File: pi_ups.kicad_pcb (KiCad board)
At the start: 2 copper layers, 92.7 x 53.3 mm, 25 parts, among them J1 Screw_Terminal_01x02, J2 Screw_Terminal_01x02, J3 Conn_02x03_Odd_Even, U1 MCP3428, U2 AP63205WU

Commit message: r0.1 board is complete
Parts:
- removed C3: 0.1u, Capacitor_SMD:C_0603_1608Metric
- removed R8: 100k, Resistor_SMD:R_0603_1608Metric
- added JP1: Jumper_2_Bridged, pi_ups:jumper_bridged_0603, B.Cu at (103.8, 97.5)
- ADR0: renamed from R7; value 0 -> Jumper_2_Bridged; footprint Resistor_SMD:R_0603_1608Metric -> pi_ups:jumper_bridged_0603; moved to B.Cu
- ADR1: renamed from R6; value 0 -> Jumper_2_Bridged; footprint Resistor_SMD:R_0603_1608Metric -> pi_ups:jumper_bridged_0603; moved to B.Cu
- J3: moved to B.Cu
- L1: footprint Inductor_SMD:L_10.4x10.4_H4.8 -> pi_ups:NRS5030
- R1, R2, R3: value 10m -> 50m
- R4: value 400k -> 1M
- moved R5 53.1 mm to (83.1, 99.8)
- moved ADR0 51.6 mm to (85.1, 91.0), turned to 90 degrees
- moved ADR1 50.9 mm to (85.1, 94.8), turned to -90 degrees
- moved U2 49.0 mm to (99.1, 94.3), turned to 90 degrees
- moved R4 48.6 mm to (83.4, 102.0), turned to 180 degrees
- moved L1 44.3 mm to (101.1, 89.4)
- moved FB1 41.6 mm to (92.7, 88.4), turned to -90 degrees
- moved C2 39.3 mm to (92.7, 91.9), turned to -90 degrees
- moved J3 39.1 mm to (109.5, 87.9), turned to 180 degrees
- moved C6 35.8 mm to (97.5, 89.9), turned to -90 degrees
- moved C1 33.3 mm to (90.2, 87.6), turned to 180 degrees
- moved C7 23.5 mm to (105.7, 92.0), turned to 90 degrees
- moved C5 22.9 mm to (102.7, 93.0)
- moved C4 19.5 mm to (103.1, 95.5)
- moved U1 9.18 mm to (87.7, 94.0)
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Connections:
- ADR0 pad 1: Net-(U1-Adr1) -> Net-(ADR0-A)
- ADR1 pad 1: Net-(U1-Adr0) -> Net-(ADR1-A)
- U1 pad 10: Net-(U1-Adr1) -> Net-(ADR1-A)
- U1 pad 9: Net-(U1-Adr0) -> Net-(ADR0-A)
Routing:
- net /GNDB: track 31.1 -> 78.6 mm
- net /SCL: track 0.00 -> 40.9 mm
- net /SDA: track 0.00 -> 35.0 mm
- net +5V: track 0.00 -> 28.3 mm
- net VCC: track 9.93 -> 35.8 mm, vias 0 -> 2
- net /Bat2_i: track 6.13 -> 31.4 mm, vias 0 -> 2
- net GND: track 0.00 -> 23.9 mm, vias 0 -> 37
- net +3.3V: track 0.00 -> 21.3 mm, vias 0 -> 1
- net Net-(JP1-A): track 0.00 -> 7.59 mm, vias 0 -> 1
- net /Bat_v: track 0.00 -> 6.76 mm
- net /Bat1_i: track 7.29 -> 13.9 mm
- net Net-(U2-SW): track 0.00 -> 5.68 mm
- net Net-(U1-VDD): track 0.00 -> 4.61 mm
- net Net-(ADR1-A): track 0.00 -> 2.79 mm, vias 0 -> 1
- net Net-(U2-BST): track 0.00 -> 2.68 mm
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- added copper zone on B.Cu, net GND
- added copper zone on F.Cu, net GND
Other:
- board size 92.7 x 53.3 mm -> 34.3 x 30 mm
- board text added: "https://github.com/kamocat/pi_ups"
- board text added: "rPi UPS v0.1 March 2023"

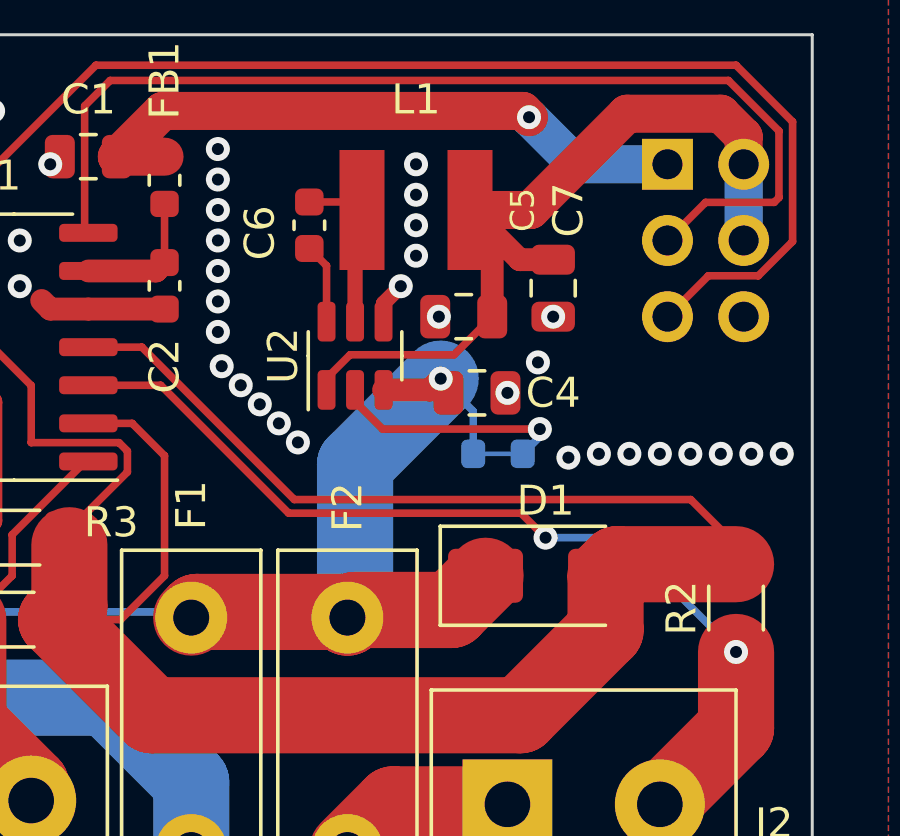
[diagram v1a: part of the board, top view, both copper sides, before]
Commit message: Minor silkscreen and package changes
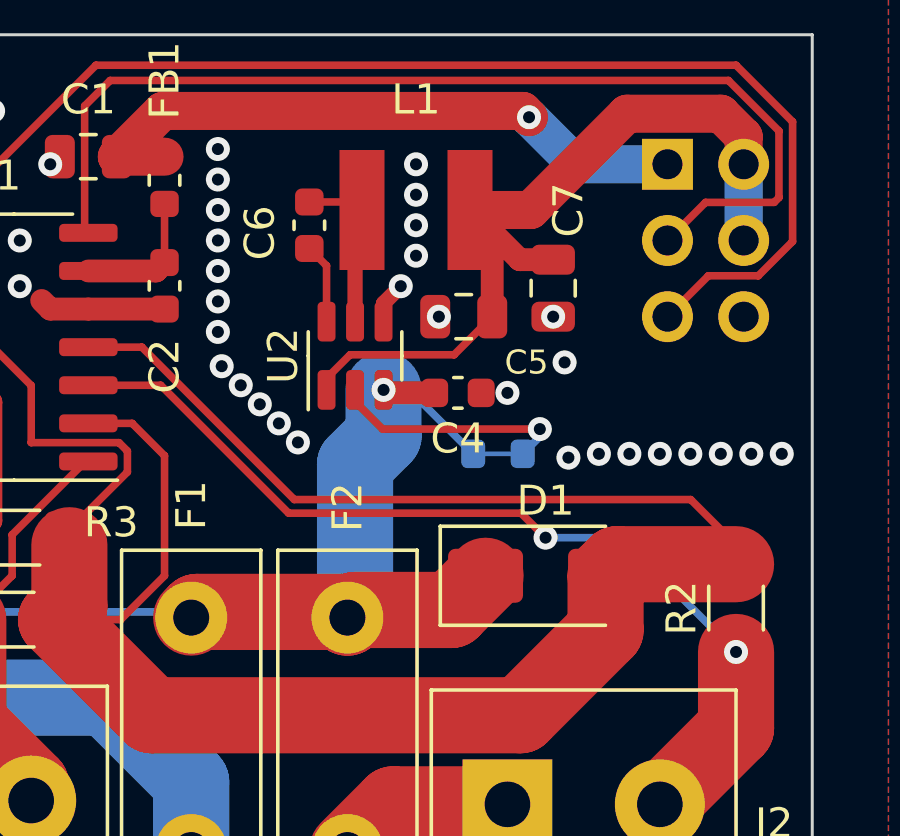
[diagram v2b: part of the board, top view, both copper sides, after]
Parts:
- C4: footprint Capacitor_SMD:C_0805_2012Metric -> Capacitor_SMD:C_0603_1608Metric
- moved C4 0.63 mm to (102.5, 95.5)
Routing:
- net VCC: track 35.8 -> 34.5 mm
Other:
- board text added: "Enable"
- board text added: "github.com/kamocat/pi_ups"
- board text removed: "https://github.com/kamocat/pi_ups"
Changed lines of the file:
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@@
     )
   )
-  (footprint "Capacitor_SMD:C_0805_2012Metric" (layer "F.Cu")
-    (at 103.124 95.504)
-    (descr "Capacitor SMD 0805 (2012 Metric), square (rectangular) end terminal, IPC_7351 nominal, (Body size source: IPC-SM-782 page 76, https://www.pcb-3d.com/wordpress/wp-content/uploads/ipc-sm-782a_amendment_1_and_2.pdf, https://docs.google.com/spreadsheets/d/1BsfQQcO9C6DZCsRaXUlFlo91Tg2WpOkGARC1WS5S8t0/edit?usp=sharing), generated with kicad-footprint-generator")
+  (footprint "Capacitor_SMD:C_0603_1608Metric" (layer "F.Cu")
+    (at 102.489 95.504)
+    (descr "Capacitor SMD 0603 (1608 Metric), square (rectangular) end terminal, IPC_7351 nominal, (Body size source: IPC-SM-782 page 76, https://www.pcb-3d.com/wordpress/wp-content/uploads/ipc-sm-782a_amendment_1_and_2.pdf), generated with kicad-footprint-generator")
     (tags "capacitor")
     (property "Sheetfile" "pi_ups.kicad_sch")
@@
     (property "ki_keywords" "cap capacitor")
     (attr smd)
-    (fp_text reference "C4" (at 2.54 0) (layer "F.SilkS")
-        (effects (font (size 1 1) (thickness 0.15)))
-    )
-    (fp_text value "10u" (at 0 1.68) (layer "F.Fab")
+    (fp_text reference "C4" (at 0 1.524) (layer "F.SilkS")
+        (effects (font (size 1 1) (thickness 0.15)))
+    )
+    (fp_text value "10u" (at 0 1.43) (layer "F.Fab")
         (effects (font (size 1 1) (thickness 0.15)))
     )
     (fp_text user "${REFERENCE}" (at 0 0) (layer "F.Fab")
-        (effects (font (size 0.5 0.5) (thickness 0.08)))
-    )
-    (fp_line (start -0.261252 -0.735) (end 0.261252 -0.735)
-      (stroke (width 0.12) (type solid)) (layer "F.SilkS"))
-    (fp_line (start -0.261252 0.735) (end 0.261252 0.735)
-      (stroke (width 0.12) (type solid)) (layer "F.SilkS"))
-    (fp_line (start -1.7 -0.98) (end 1.7 -0.98)
-      (stroke (width 0.05) (type solid)) (layer "F.CrtYd"))
-    (fp_line (start -1.7 0.98) (end -1.7 -0.98)
-      (stroke (width 0.05) (type solid)) (layer "F.CrtYd"))
-    (fp_line (start 1.7 -0.98) (end 1.7 0.98)
-      (stroke (width 0.05) (type solid)) (layer "F.CrtYd"))
-    (fp_line (start 1.7 0.98) (end -1.7 0.98)
-      (stroke (width 0.05) (type solid)) (layer "F.CrtYd"))
-    (fp_line (start -1 -0.625) (end 1 -0.625)
-      (stroke (width 0.1) (type solid)) (layer "F.Fab"))
-    (fp_line (start -1 0.625) (end -1 -0.625)
-      (stroke (width 0.1) (type solid)) (layer "F.Fab"))
-    (fp_line (start 1 -0.625) (end 1 0.625)
-      (stroke (width 0.1) (type solid)) (layer "F.Fab"))
-    (fp_line (start 1 0.625) (end -1 0.625)
-      (stroke (width 0.1) (type solid)) (layer "F.Fab"))
-    (pad "1" smd roundrect (at -0.95 0) (size 1 1.45) (layers "F.Cu" "F.Paste" "F.Mask") (roundrect_rratio 0.25)
+        (effects (font (size 0.4 0.4) (thickness 0.06)))
+    )
+    (fp_line (start -0.14058 -0.51) (end 0.14058 -0.51)
+      (stroke (width 0.12) (type solid)) (layer "F.SilkS"))
+    (fp_line (start -0.14058 0.51) (end 0.14058 0.51)
+      (stroke (width 0.12) (type solid)) (layer "F.SilkS"))
+    (fp_line (start -1.48 -0.73) (end 1.48 -0.73)
+      (stroke (width 0.05) (type solid)) (layer "F.CrtYd"))
+    (fp_line (start -1.48 0.73) (end -1.48 -0.73)
+      (stroke (width 0.05) (type solid)) (layer "F.CrtYd"))
+    (fp_line (start 1.48 -0.73) (end 1.48 0.73)
+      (stroke (width 0.05) (type solid)) (layer "F.CrtYd"))
+    (fp_line (start 1.48 0.73) (end -1.48 0.73)
+      (stroke (width 0.05) (type solid)) (layer "F.CrtYd"))
+    (fp_line (start -0.8 -0.4) (end 0.8 -0.4)
+      (stroke (width 0.1) (type solid)) (layer "F.Fab"))
+    (fp_line (start -0.8 0.4) (end -0.8 -0.4)
+      (stroke (width 0.1) (type solid)) (layer "F.Fab"))
+    (fp_line (start 0.8 -0.4) (end 0.8 0.4)
+      (stroke (width 0.1) (type solid)) (layer "F.Fab"))
+    (fp_line (start 0.8 0.4) (end -0.8 0.4)
+      (stroke (width 0.1) (type solid)) (layer "F.Fab"))
+    (pad "1" smd roundrect (at -0.775 0) (size 0.9 0.95) (layers "F.Cu" "F.Paste" "F.Mask") (roundrect_rratio 0.25)
       (net 1 "VCC") (pintype "passive"))
-    (pad "2" smd roundrect (at 0.95 0) (size 1 1.45) (layers "F.Cu" "F.Paste" "F.Mask") (roundrect_rratio 0.25)
+    (pad "2" smd roundrect (at 0.775 0) (size 0.9 0.95) (layers "F.Cu" "F.Paste" "F.Mask") (roundrect_rratio 0.25)
       (net 2 "GND") (pintype "passive"))
-    (model "${KICAD6_3DMODEL_DIR}/Capacitor_SMD.3dshapes/C_0805_2012Metric.wrl"
+    (model "${KICAD6_3DMODEL_DIR}/Capacitor_SMD.3dshapes/C_0603_1608Metric.wrl"
       (offset (xyz 0 0 0))
       (scale (xyz 1 1 1))
@@
     (property "ki_keywords" "cap capacitor")
     (attr smd)
-    (fp_text reference "C5" (at 1.966 -3.556 90) (layer "F.SilkS")
+    (fp_text reference "C5" (at 2.093 1.524 180) (layer "F.SilkS")
         (effects (font (size 0.8 0.8) (thickness 0.1)))
     )
@@
     (property "ki_keywords" "Jumper SPST")
     (attr smd)
-    (fp_text reference "JP1" (at 0 1.43) (layer "B.SilkS")
+    (fp_text reference "JP1" (at 0 -1.524) (layer "B.SilkS") hide
         (effects (font (size 1 1) (thickness 0.15)) (justify mirror))
     )
@@
     (property "ki_keywords" "connector")
     (attr through_hole)
-    (fp_text reference "J3" (at -1.27 2.77) (layer "B.SilkS")
+    (fp_text reference "J3" (at -1.397 -7.747) (layer "B.SilkS")
         (effects (font (size 1 1) (thickness 0.15)) (justify mirror))
     )
@@
   (gr_rect (start 80.01 83.566) (end 114.3 113.538)
     (stroke (width 0.1) (type default)) (fill none) (layer "Edge.Cuts"))
-  (gr_text "https://github.com/kamocat/pi_ups" (at 110.49 85.217) (layer "B.SilkS")
+  (gr_text "github.com/kamocat/pi_ups" (at 107.188 85.344) (layer "B.SilkS")
+    (effects (font (size 1 1) (thickness 0.15)) (justify left bottom mirror))
+  )
+  (gr_text "Enable" (at 106.045 99.568) (layer "B.SilkS")
     (effects (font (size 1 1) (thickness 0.15)) (justify left bottom mirror))
   )
@@
   (segment (start 102.27 102.74) (end 103.41 101.6) (width 2.54) (layer "F.Cu") (net 1))
   (segment (start 93.599 102.994) (end 93.788 102.805) (width 2.54) (layer "F.Cu") (net 1))
-  (segment (start 101.54 95.405) (end 102.075 95.405) (width 0.762) (layer "F.Cu") (net 1))
   (segment (start 84.264 101.981) (end 84.582 101.981) (width 0.254) (layer "F.Cu") (net 1))
+  (segment (start 100.109 95.504) (end 100.01 95.405) (width 0.762) (layer "F.Cu") (net 1))
   (segment (start 84.582 101.981) (end 85.217 101.346) (width 0.254) (layer "F.Cu") (net 1))
-  (segment (start 101.54 95.405) (end 101.915 95.03) (width 0.762) (layer "F.Cu") (net 1))
   (segment (start 98.617 102.805) (end 98.806 102.994) (width 2.54) (layer "F.Cu") (net 1))
   (segment (start 93.788 102.805) (end 98.617 102.805) (width 2.54) (layer "F.Cu") (net 1))
   (segment (start 99.06 102.74) (end 102.27 102.74) (width 2.54) (layer "F.Cu") (net 1))
-  (segment (start 100.01 95.405) (end 101.54 95.405) (width 0.762) (layer "F.Cu") (net 1))
-  (segment (start 102.075 95.405) (end 102.174 95.504) (width 0.762) (layer "F.Cu") (net 1))
+  (segment (start 101.714 95.504) (end 100.109 95.504) (width 0.762) (layer "F.Cu") (net 1))
   (via (at 85.217 101.346) (size 0.8) (drill 0.4) (layers "F.Cu" "B.Cu") (net 1))
-  (via (at 101.915 95.03) (size 0.8) (drill 0.4) (layers "F.Cu" "B.Cu") (net 1))
-  (segment (start 99.06 102.74) (end 99.06 97.885) (width 2.54) (layer "B.Cu") (net 1))
+  (via (at 100.01 95.405) (size 0.8) (drill 0.4) (layers "F.Cu" "B.Cu") (net 1))
   (segment (start 93.599 102.994) (end 93.41 102.805) (width 0.254) (layer "B.Cu") (net 1))
   (segment (start 86.676 102.805) (end 85.217 101.346) (width 0.254) (layer "B.Cu") (net 1))
   (segment (start 93.41 102.805) (end 86.676 102.805) (width 0.254) (layer "B.Cu") (net 1))
-  (segment (start 99.06 97.885) (end 101.915 95.03) (width 2.54) (layer "B.Cu") (net 1))
-  (segment (start 102.998 97.536) (end 102.998 96.113) (width 0.254) (layer "B.Cu") (net 1))
-  (segment (start 98.806 102.994) (end 99.06 102.74) (width 2.54) (layer "B.Cu") (net 1))
-  (segment (start 102.998 96.113) (end 101.915 95.03) (width 0.254) (layer "B.Cu") (net 1))
+  (segment (start 99.06 97.885) (end 99.06 102.74) (width 2.54) (layer "B.Cu") (net 1))
+  (segment (start 100.867 95.405) (end 102.998 97.536) (width 0.254) (layer "B.Cu") (net 1))
+  (segment (start 100.01 95.405) (end 100.867 95.405) (width 0.254) (layer "B.Cu") (net 1))
+  (segment (start 99.06 102.74) (end 98.806 102.994) (width 2.54) (layer "B.Cu") (net 1))
+  (segment (start 100.01 95.405) (end 100.01 96.935) (width 2.54) (layer "B.Cu") (net 1))
+  (segment (start 100.01 96.935) (end 99.06 97.885) (width 2.54) (layer "B.Cu") (net 1))
   (segment (start 100.01 92.522) (end 100.584 91.948) (width 0.508) (layer "F.Cu") (net 2))
   (segment (start 89.22 87.63) (end 88.9 87.884) (width 0.762) (layer "F.Cu") (net 2))
@@
   (via (at 106.172 97.663) (size 0.8) (drill 0.4) (layers "F.Cu" "B.Cu") (free) (net 2))
   (via (at 109.22 97.536) (size 0.8) (drill 0.4) (layers "F.Cu" "B.Cu") (free) (net 2))
-  (via (at 105.156 94.488) (size 0.8) (drill 0.4) (layers "F.Cu" "B.Cu") (free) (net 2))
+  (via (at 106.045 94.488) (size 0.8) (drill 0.4) (layers "F.Cu" "B.Cu") (free) (net 2))
   (via (at 104.14 95.504) (size 0.8) (drill 0.4) (layers "F.Cu" "B.Cu") (net 2))
   (via (at 108.204 97.536) (size 0.8) (drill 0.4) (layers "F.Cu" "B.Cu") (free) (net 2))
